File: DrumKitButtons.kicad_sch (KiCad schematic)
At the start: 25 parts, among them J1 Input, J2 Output, U1 74HC165, U2 TLC5916

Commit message: next revision
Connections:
- net GND: no longer SW1.6 (GND), SW2.6 (GND), SW3.6 (GND), SW4.6 (GND), SW5.6 (GND), SW6.6 (GND), SW7.6 (GND), SW8.6 (GND)
- net LED_{1}: now also SW1.6 (LED-); no longer SW1.5 (LED+)
- net LED_{2}: now also SW2.6 (LED-); no longer SW2.5 (LED+)
- net LED_{3}: now also SW3.6 (LED-); no longer SW3.5 (LED+)
- net LED_{4}: now also SW4.6 (LED-); no longer SW4.5 (LED+)
- net LED_{5}: now also SW5.6 (LED-); no longer SW5.5 (LED+)
- net LED_{6}: now also SW6.6 (LED-); no longer SW6.5 (LED+)
- net LED_{7}: now also SW7.6 (LED-); no longer SW7.5 (LED+)
- net LED_{8}: now also SW8.6 (LED-); no longer SW8.5 (LED+)
- net VCC: now also SW1.5 (LED+), SW2.5 (LED+), SW3.5 (LED+), SW4.5 (LED+), SW5.5 (LED+), SW6.5 (LED+), SW7.5 (LED+), SW8.5 (LED+)
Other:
- moved on the sheet: R1, SW1

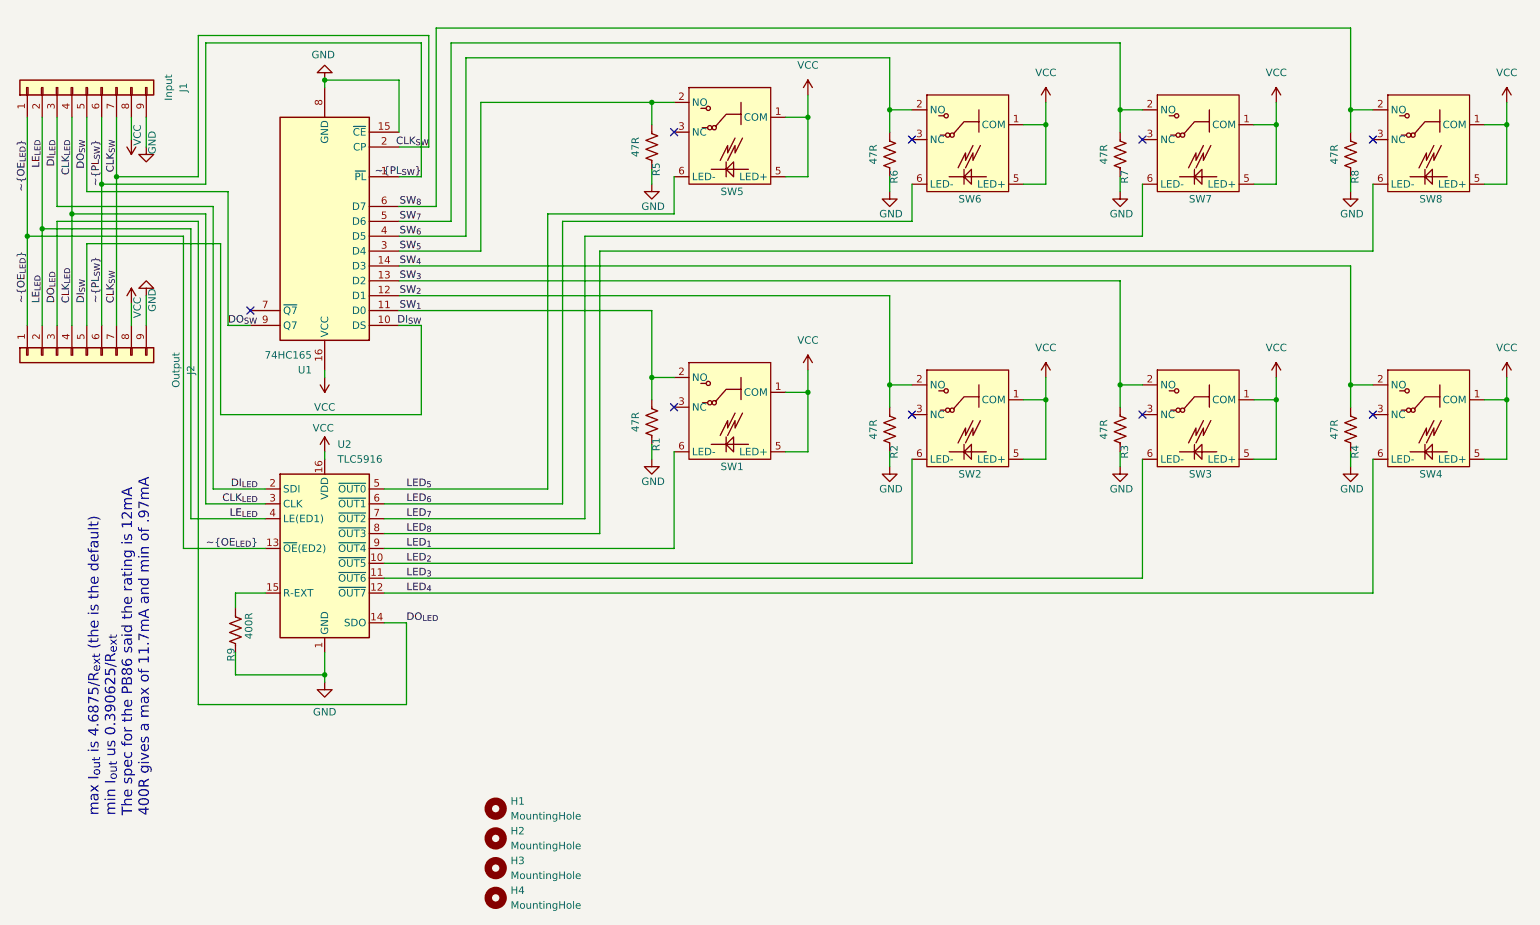
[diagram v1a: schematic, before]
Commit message: 2 banks of 8 buttons; ICs on left
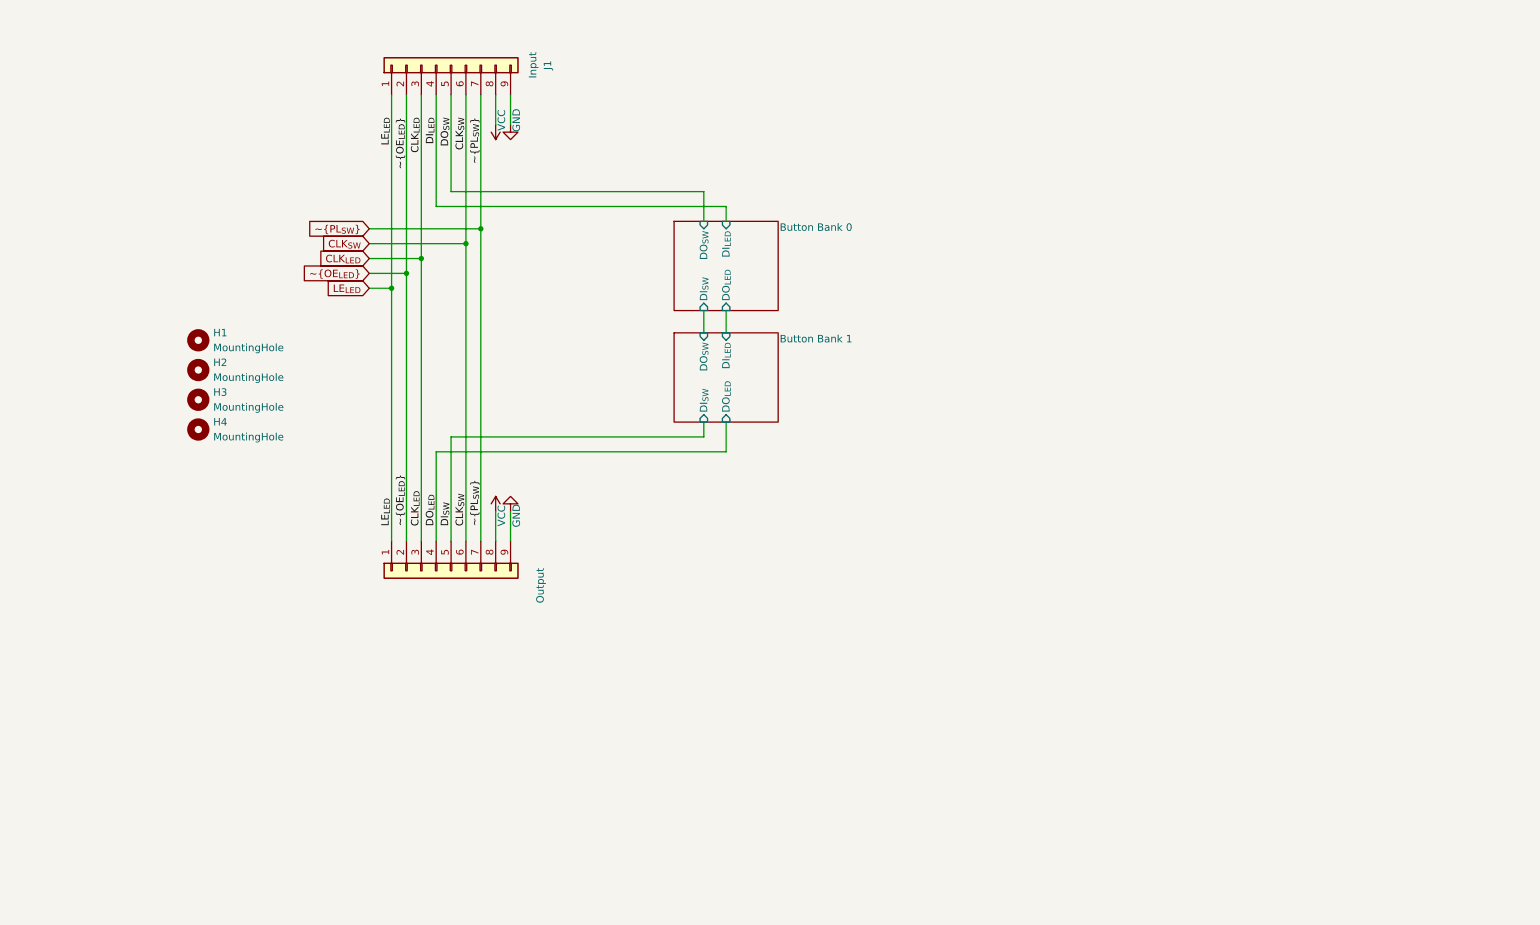
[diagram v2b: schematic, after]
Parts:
- removed R1, R2, R3, R4, R5, R6, R7, R8: 47R, Resistor_THT:R_Axial_DIN0204_L3.6mm_D1.6mm_P5.08mm_Horizontal, symbol Device:R_US
- removed R9: 400R, Resistor_THT:R_Axial_DIN0204_L3.6mm_D1.6mm_P5.08mm_Horizontal, symbol Device:R_US
- removed SW1, SW2, SW3, SW4, SW5, SW6, SW7, SW8: ~, Local:PB86, symbol Local:PB68
- removed U1: 74HC165, Package_DIP:DIP-16_W7.62mm, symbol 74xx:74HC165
- removed U2: TLC5916, Package_DIP:DIP-16_W7.62mm, symbol Driver_LED:TLC5916
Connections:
- net CLK_{LED}: now also J1.3 (Pin_3), J2.3 (Pin_3); no longer J1.4 (Pin_4), J2.4 (Pin_4)
- net CLK_{SW}: now also J1.6 (Pin_6), J2.6 (Pin_6); no longer J1.7 (Pin_7), J2.7 (Pin_7)
- net DI_{LED}: now also J1.4 (Pin_4); no longer J1.3 (Pin_3)
- net DO_{LED}: now also J2.4 (Pin_4); no longer J2.3 (Pin_3)
- net LE_{LED}: now also J1.1 (Pin_1), J2.1 (Pin_1); no longer J1.2 (Pin_2), J2.2 (Pin_2)
- net ~{OE_{LED}}: now also J1.2 (Pin_2), J2.2 (Pin_2); no longer J1.1 (Pin_1), J2.1 (Pin_1)
- net ~{PL_{SW}}: now also J1.7 (Pin_7), J2.7 (Pin_7); no longer J1.6 (Pin_6), J2.6 (Pin_6)
- no-connect marks 9 -> 0
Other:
- added sheet Button Bank 0 (8-buttons.kicad_sch)
- added sheet Button Bank 1 (8-buttons.kicad_sch)
- moved on the sheet: H1, H2, H3, H4, J1
